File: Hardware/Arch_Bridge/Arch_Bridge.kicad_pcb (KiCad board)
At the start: 2 copper layers, 88.8 x 76 mm, 99 parts, among them J1 Conn_01x02, J3 Conn_01x04, J4 Conn_01x04, Q1 MMBT3904, Q2 MMBT3906, Q3 MJE2955, U1 AP63205WU, U10 74LVC1G04, U11 ESP32-S3-WROOM-1, U12 TXS0102DCT, U13 DRV8231ADDAR, U14 74LVC1G3208, U15 74LVC1G3208, U16 74LVC1G04, U17 TXS0102DCT, U18 TXS0102DCT, U19 TXS0108EPW, U2 TLV1117LV33DCYR, U20 TXS0108EPW, U3 LM393B, U4 74LVC1G04, U5 74LVC1G02, U6 TLP2770, U7 DRV8231ADDAR, U8 74LVC1G3208, U9 74LVC1G3208

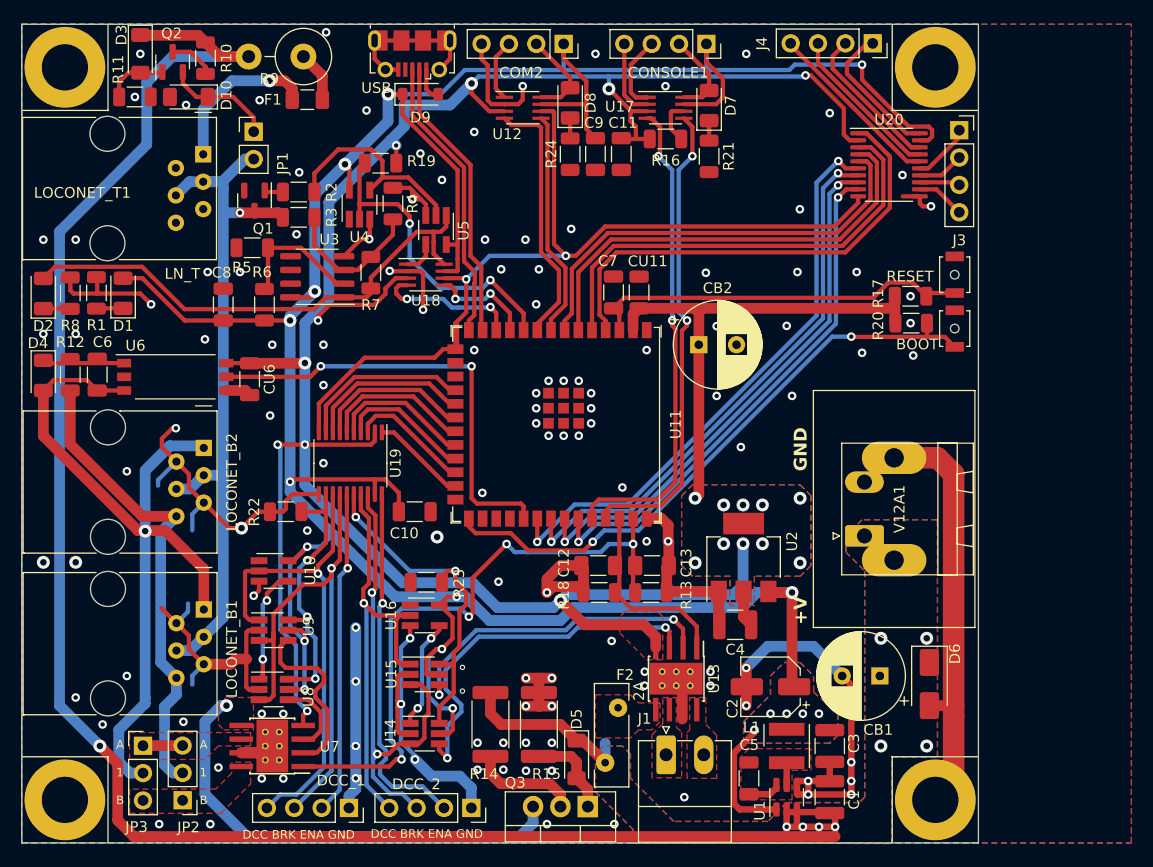
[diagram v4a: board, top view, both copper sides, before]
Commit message: Revised PCB to fix thermal problems, improve usage of board space. DCC inputs, serial ports, and GPIO all have independent IOREF connections.
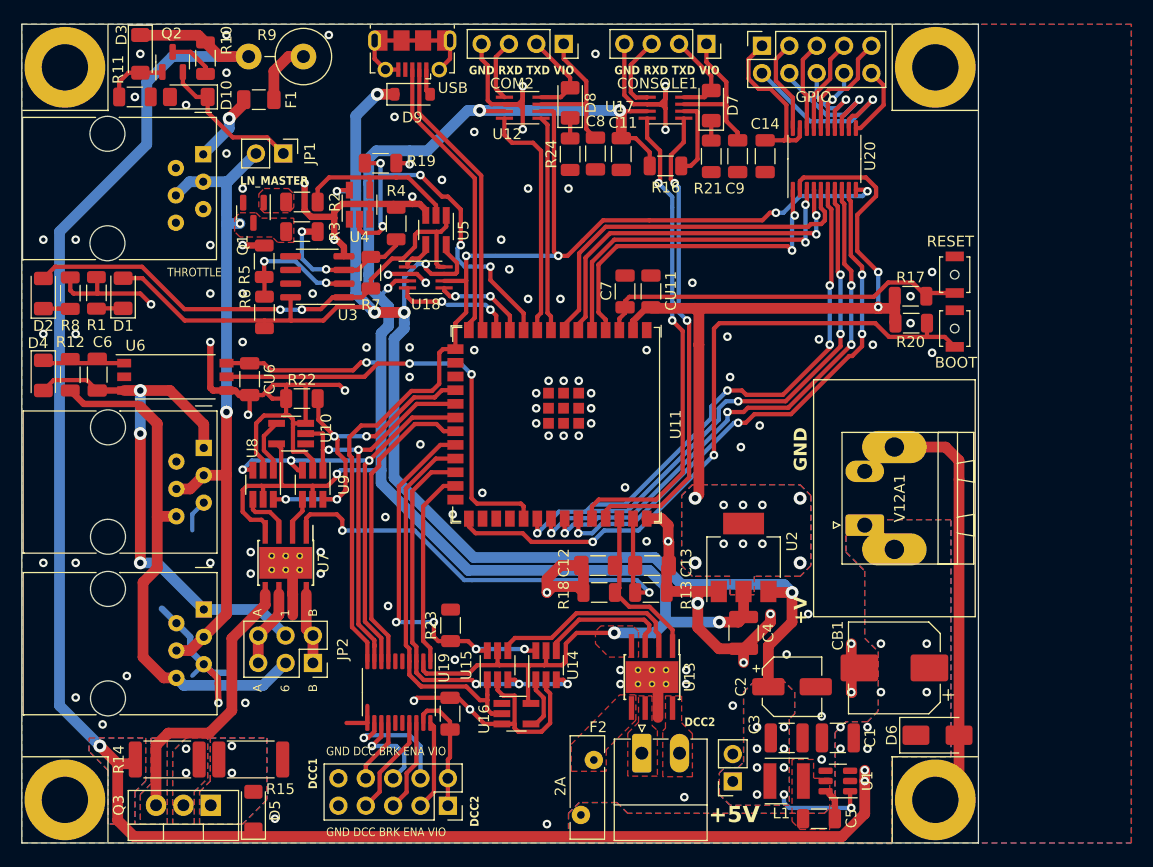
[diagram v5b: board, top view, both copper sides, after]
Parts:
- removed CB2: 100uF, Capacitor_THT:CP_Radial_D8.0mm_P3.50mm
- removed DCC_1, DCC_2: Conn_01x04_Female, Connector_PinSocket_2.54mm:PinSocket_1x04_P2.54mm_Vertical
- removed J3, J4: Conn_01x04, Connector_PinSocket_2.54mm:PinSocket_1x04_P2.54mm_Vertical
- removed JP3: Jumper_NC_Dual, Connector_PinHeader_2.54mm:PinHeader_1x03_P2.54mm_Vertical
- added C14: 0.1uF, Capacitor_SMD:C_1206_3216Metric, F.Cu at (89.0, 32.2)
- added DCC1: Conn_02x05_Odd_Even, Connector_PinSocket_2.54mm:PinSocket_2x05_P2.54mm_Vertical, F.Cu at (59.5, 92.5)
- added GPIO: Conn_02x05_Odd_Even, Connector_PinSocket_2.54mm:PinSocket_2x05_P2.54mm_Vertical, F.Cu at (88.7, 22.0)
- added J5V1: Conn_01x02, Connector_PinSocket_2.54mm:PinSocket_1x02_P2.54mm_Vertical, F.Cu at (86.0, 90.3)
- CB1: footprint Capacitor_THT:CP_Radial_D8.0mm_P3.50mm -> Capacitor_SMD:CP_Elec_8x10
- JP2: value Jumper_NC_Dual -> Conn_02x03_Odd_Even; footprint Connector_PinHeader_2.54mm:PinHeader_1x03_P2.54mm_Vertical -> Connector_PinSocket_2.54mm:PinSocket_2x03_P2.54mm_Vertical
- moved C8 37.3 mm to (73.2, 32.0), turned to -90 degrees
- moved Q3 35.0 mm to (37.5, 92.5)
- moved D5 30.4 mm to (41.5, 93.0), turned to 90 degrees
- moved R14 30.2 mm to (33.5, 88.2), turned to 180 degrees
- moved R15 26.9 mm to (41.2, 88.2), turned to 0 degrees
- moved U19 21.7 mm to (55.0, 82.0)
- moved C10 19.0 mm to (59.8, 84.0), turned to 90 degrees
- moved U8 19.0 mm to (42.4, 62.8), turned to -90 degrees
- moved JP2 17.6 mm to (47.0, 79.3), turned to -90 degrees
- moved U7 17.0 mm to (44.5, 70.0), turned to -90 degrees
- moved U9 14.0 mm to (47.0, 62.8), turned to -90 degrees
- moved C9 13.2 mm to (86.5, 32.2)
- moved U14 12.9 mm to (68.7, 79.5), turned to 90 degrees
- moved U10 12.9 mm to (45.0, 58.0), turned to 180 degrees
- moved U16 12.5 mm to (65.9, 84.0)
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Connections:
- C10 pad 1: +5V -> Net-(DCC1-Pin_1)
- C7 pad 1: /RESET -> GND
- C7 pad 2: GND -> /RESET
- C8 pad 1: +5V -> /VCOM2
- C9 pad 1: +5V -> /VCOM1
- COM2 pad 1: +5V -> /VCOM2
- CONSOLE1 pad 1: +5V -> /VCOM1
- D2 pad 2: Net-(D2-A) -> /LN_RX
- JP2 pad 2: /LN_B6 -> /OUT1_B
- JP2 pad 3: /OUT1_A -> /LN_B6
- R15 pad 1: GND -> Net-(D5-A)
- R15 pad 2: Net-(D5-A) -> GND
- R7 pad 1: Net-(D2-A) -> /LN_RX
- U10 pad 5: +5V -> +3.3V
- U11 pad 11: /LN_RX -> Net-(U11-GPIO18/U1RXD/ADC2_CH7/CLK_OUT3)
- U11 pad 12: /LN_COLL -> Net-(U11-GPIO8/TOUCH8/ADC1_CH7/SUBSPICS1)
- U11 pad 18: Net-(U11-GPIO10/TOUCH10/ADC1_CH9/FSPICS0/FSPIIO4/SUBSPICS0) -> /ENA_1o
- U11 pad 19: Net-(U11-GPIO11/TOUCH11/ADC2_CH0/FSPID/FSPIIO5/SUBSPID) -> /DCC_1
- U11 pad 20: Net-(U11-GPIO12/TOUCH12/ADC2_CH1/FSPICLK/FSPIIO6/SUBSPICLK) -> /BRK_1
- U11 pad 21: Net-(U11-GPIO13/TOUCH13/ADC2_CH2/FSPIQ/FSPIIO7/SUBSPIQ) -> /ENA_1i
- U11 pad 22: Net-(U11-GPIO14/TOUCH14/ADC2_CH3/FSPIWP/FSPIDQS/SUBSPIWP) -> /ENA_2o
- U11 pad 23: Net-(U11-GPIO21) -> /DCC_2
- U11 pad 24: Net-(U11-GPIO47/SPICLK_P/SUBSPICLK_P_DIFF) -> /BRK_2
- U11 pad 25: Net-(U11-GPIO48/SPICLK_N/SUBSPICLK_N_DIFF) -> /ENA_2i
- U12 pad 7: +5V -> /VCOM2
- U14 pad 5: +5V -> +3.3V
- U15 pad 5: +5V -> +3.3V
- U16 pad 5: +5V -> +3.3V
- U17 pad 7: +5V -> /VCOM1
- U18 pad 1: Net-(U18-B2) -> /LN_COLL
- U18 pad 4: /LN_COLL -> Net-(U11-GPIO8/TOUCH8/ADC1_CH7/SUBSPICS1)
- U18 pad 5: /LN_RX -> Net-(U11-GPIO18/U1RXD/ADC2_CH7/CLK_OUT3)
- U18 pad 8: Net-(D2-A) -> /LN_RX
- U19 pad 1: Net-(U11-GPIO48/SPICLK_N/SUBSPICLK_N_DIFF) -> /ENA_2i
- U19 pad 12: /ENA_1o -> Net-(DCC1-Pin_4)
- U19 pad 13: /DCC_1 -> Net-(DCC1-Pin_6)
- U19 pad 14: /BRK_1 -> Net-(DCC1-Pin_8)
- U19 pad 15: /ENA_1i -> unconnected-(U19-B5-Pad15)
- U19 pad 16: /ENA_2o -> unconnected-(U19-B4-Pad16)
- U19 pad 17: /DCC_2 -> Net-(DCC1-Pin_7)
- U19 pad 18: /BRK_2 -> Net-(DCC1-Pin_5)
- U19 pad 19: +5V -> Net-(DCC1-Pin_1)
- U19 pad 20: /ENA_2i -> Net-(DCC1-Pin_3)
- U19 pad 3: Net-(U11-GPIO47/SPICLK_P/SUBSPICLK_P_DIFF) -> /BRK_2
- U19 pad 4: Net-(U11-GPIO21) -> /DCC_2
- U19 pad 5: Net-(U11-GPIO14/TOUCH14/ADC2_CH3/FSPIWP/FSPIDQS/SUBSPIWP) -> unconnected-(U19-A4-Pad5)
- U19 pad 6: Net-(U11-GPIO13/TOUCH13/ADC2_CH2/FSPIQ/FSPIIO7/SUBSPIQ) -> unconnected-(U19-A5-Pad6)
- U19 pad 7: Net-(U11-GPIO12/TOUCH12/ADC2_CH1/FSPICLK/FSPIIO6/SUBSPICLK) -> /ENA_1i
- U19 pad 8: Net-(U11-GPIO11/TOUCH11/ADC2_CH0/FSPID/FSPIIO5/SUBSPID) -> /BRK_1
- U19 pad 9: Net-(U11-GPIO10/TOUCH10/ADC1_CH9/FSPICS0/FSPIIO4/SUBSPICS0) -> /DCC_1
- U20 pad 19: +5V -> Net-(DCC2-Pin_1)
- U3 pad 1: Net-(D2-A) -> /LN_RX
- U5 pad 1: Net-(D2-A) -> /LN_RX
- U5 pad 4: Net-(U18-B2) -> /LN_COLL
- U8 pad 5: +5V -> +3.3V
- U9 pad 5: +5V -> +3.3V
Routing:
- net +5V: track 306.5 -> 147.0 mm, vias 18 -> 15
- net Net-(D2-A): track 47.9 -> 0.00 mm
- net /LN_RX: track 9.62 -> 48.5 mm
- net /LN_B1: track 76.4 -> 51.5 mm, vias 1 -> 3
- net +12V: track 195.3 -> 172.1 mm, vias 9 -> 11
- net Net-(U13-IN1): track 35.0 -> 12.6 mm, vias 2 -> 0
- net /OE: track 83.8 -> 103.1 mm, vias 2 -> 4
- net Net-(Q3-E): track 43.5 -> 26.0 mm, vias 1 -> 0
- net Net-(U11-GPIO10/TOUCH10/ADC1_CH9/FSPICS0/FSPIIO4/SUBSPICS0): track 16.1 -> 0.00 mm
- net Net-(DCC2-Pin_1): track 0.00 -> 16.1 mm
- net /ENA_2i: track 33.9 -> 18.4 mm, vias 1 -> 0
- net Net-(U11-GPIO11/TOUCH11/ADC2_CH0/FSPID/FSPIIO5/SUBSPID): track 15.4 -> 0.00 mm
- net GND: track 287.7 -> 272.6 mm, vias 129 -> 110
- net Net-(U11-GPIO12/TOUCH12/ADC2_CH1/FSPICLK/FSPIIO6/SUBSPICLK): track 14.6 -> 0.00 mm
- net /VCOM2: track 0.00 -> 14.2 mm
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- added copper zone on F.Cu, net /LN_DAT
- added copper zone on B.Cu, net Net-(D5-A)
- added copper zone on F.Cu, net Net-(D5-A)
- added copper zone on F.Cu, net Net-(Q1-B)
- added copper zone on B.Cu, net Net-(Q3-C)
- added copper zone on F.Cu, net Net-(Q3-C)
- added copper zone on B.Cu, net Net-(Q3-E)
- removed copper zone on F.Cu, net /OUT1_A
- removed copper zone on F.Cu, net /OUT1_B
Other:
- board text added: "+5V"
- board text added: "A 6 B"
- board text added: "DCC1"
- board text added: "DCC2"
- board text added: "GND DCC BRK ENA VIO"
- board text added: "GND RXD TXD VIO"
- board text added: "LN_MASTER"
- board text added: "THROTTLE"
- board text removed: "DCC BRK ENA GND"
- board text removed: "LN_T"

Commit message: Board revision progress
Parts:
- added R25: 10k, Resistor_SMD:R_1206_3216Metric, F.Cu at (68.5, 39.8)
- CONSOLE1: value Conn_01x03 -> Conn_01x04
- D10: value Z-12 -> Z-13
- R9: value 33 2w -> 33 3w
- renumbered GPIO to DCC2
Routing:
- net GND: track 272.6 -> 296.1 mm, vias 110 -> 111
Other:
- board text added: "GPIO"

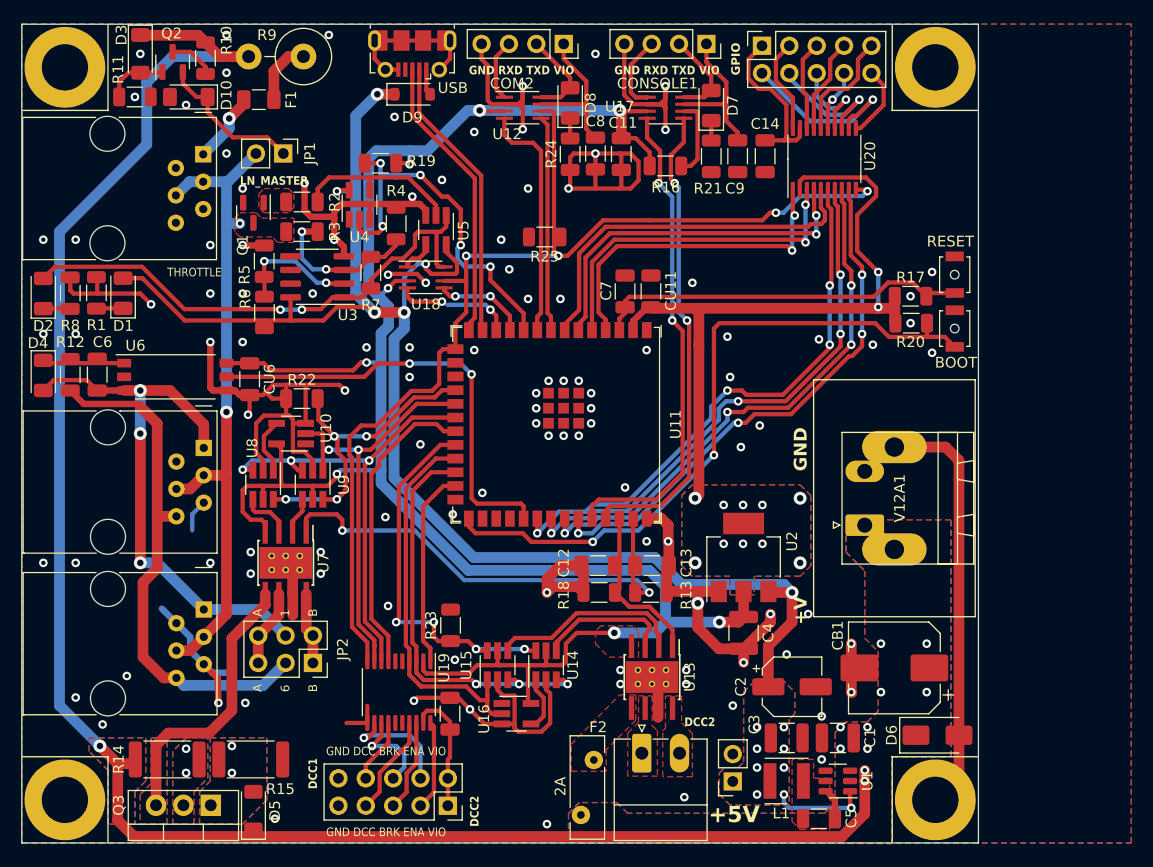
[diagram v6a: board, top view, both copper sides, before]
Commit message: Added Railsync voltage monitoring circuit, stabilizer cap. Updated BOM with new parts.
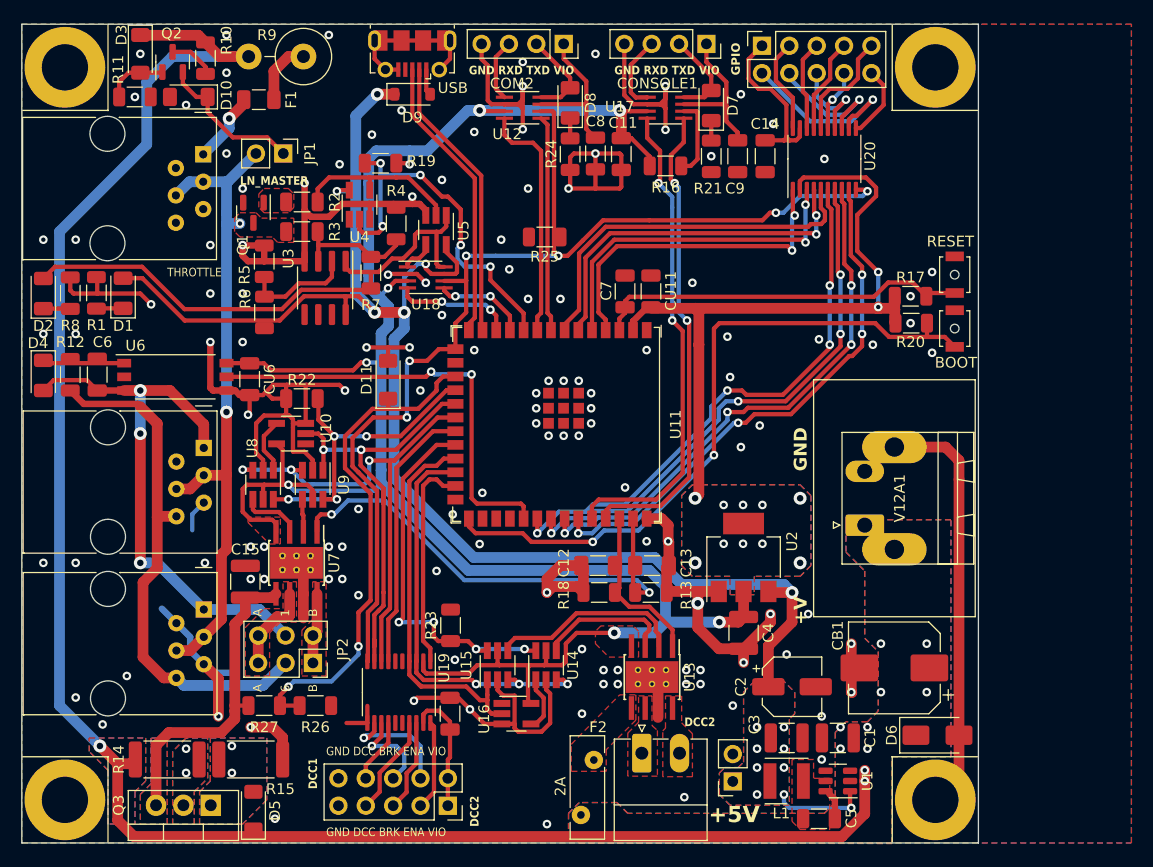
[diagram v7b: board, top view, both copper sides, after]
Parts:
- added C15: 10uF, Capacitor_SMD:C_1210_3225Metric, F.Cu at (40.8, 71.8)
- added D11: 3.3v, Diode_SMD:D_MiniMELF, F.Cu at (54.0, 53.0)
- added R26: 3k, Resistor_SMD:R_1206_3216Metric, F.Cu at (47.2, 83.2)
- added R27: 22k, Resistor_SMD:R_1206_3216Metric, F.Cu at (42.5, 83.2)
- moved U3 1.26 mm to (48.2, 44.5), turned to -90 degrees
- moved U7 1.00 mm to (45.5, 70.0)
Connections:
- net Net-(Q3-E) renamed /VM1
- net Net-(U13-VM) renamed /VM2
- U11 pad 17: unconnected-(U11-GPIO9/TOUCH9/ADC1_CH8/FSPIHD/SUBSPIHD-Pad17) -> /VMS1
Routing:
- net /VMS1: track 0.00 -> 47.3 mm, vias 0 -> 2
- net GND: track 296.1 -> 311.5 mm, vias 111 -> 128
- net /VM1: track 26.0 -> 29.8 mm
- net /LN_RX: track 48.5 -> 52.1 mm, vias 2 -> 0
- net /ENA_1i: track 28.4 -> 25.2 mm
- net Net-(U3A-+): track 14.6 -> 11.5 mm, vias 2 -> 0
- net +3.3V: track 257.8 -> 260.3 mm
- net /DCC_1: track 39.5 -> 41.6 mm
- net /ENA_2i: track 18.4 -> 20.1 mm
- net /OE: track 103.1 -> 104.7 mm, vias 4 -> 6
- net Net-(U3A--): track 11.6 -> 10.3 mm, vias 2 -> 0
- net /BRK_1: track 43.8 -> 44.9 mm
- net /OUT1_A: track 7.21 -> 8.24 mm
- net Net-(U7-IN1): track 4.82 -> 5.73 mm
- net /ENA_1o: track 30.9 -> 30.2 mm
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- added copper zone on F.Cu, net /OUT1_A
- added copper zone on F.Cu, net /OUT1_B

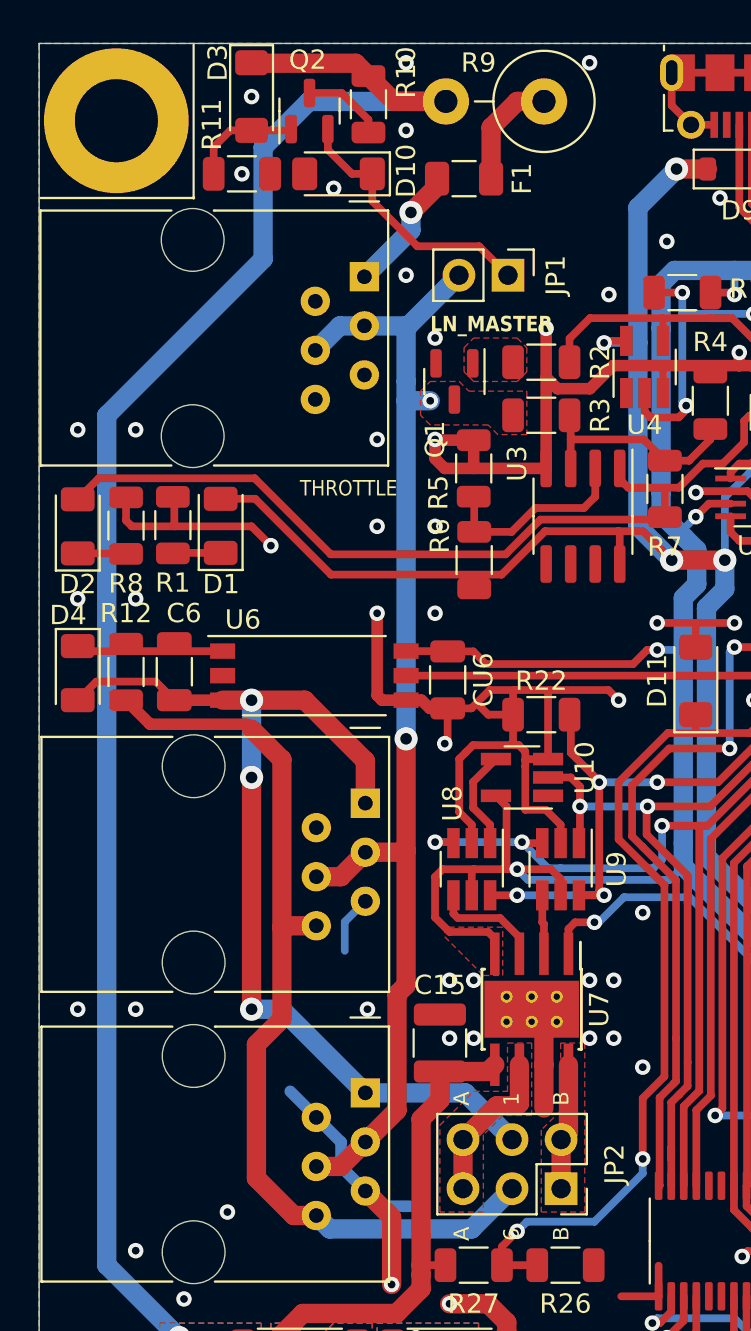
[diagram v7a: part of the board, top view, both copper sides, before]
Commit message: Fixed BOM error for JP2, should have been 2x3 pin header not socket.
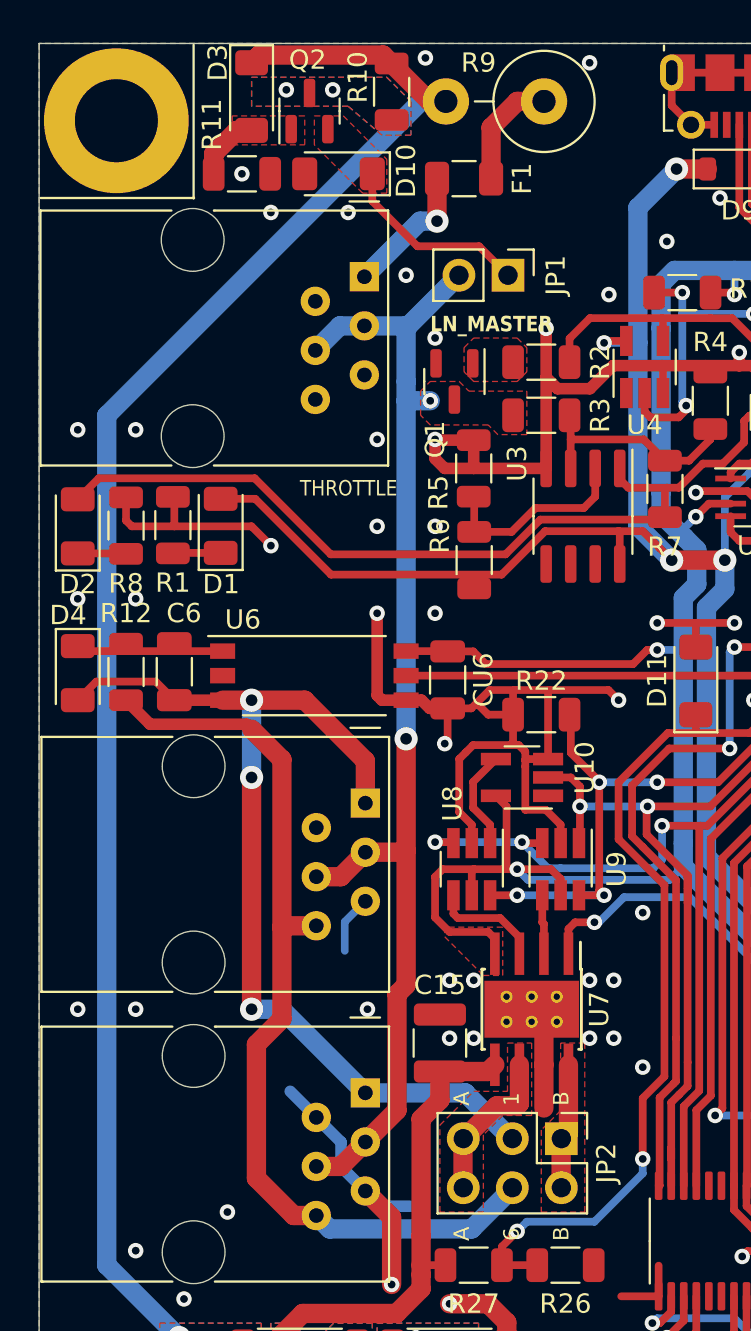
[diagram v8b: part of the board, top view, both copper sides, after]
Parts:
- JP2: footprint Connector_PinSocket_2.54mm:PinSocket_2x03_P2.54mm_Vertical -> Connector_PinHeader_2.54mm:PinHeader_2x03_P2.54mm_Vertical
- R22, R23: value 47k -> 150k
- U19, U20: value TXS0108EPW -> TXB0108PWR
- U5: value 74LVC1G02 -> 74LVC1G86
- moved JP2 2.59 mm to (47.0, 76.7)
- moved R10 1.36 mm to (38.2, 22.5)
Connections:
- JP2 pad 3: /LN_B6 -> /LN_B1
- JP2 pad 4: /LN_B1 -> /LN_B6
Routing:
- net Net-(Q2-C): track 4.29 -> 0.00 mm, vias 0 -> 2
- net Net-(D10-K): track 13.9 -> 10.0 mm
- net +12V: track 172.1 -> 169.1 mm
- net Net-(D3-A): track 5.78 -> 3.59 mm
- net /T_PWR: track 6.64 -> 7.15 mm
- net GND: vias 128 -> 127
- added copper zone on F.Cu, net Net-(D10-K)
- added copper zone on F.Cu, net Net-(D3-A)
- added copper zone on B.Cu, net Net-(Q2-C)
- added copper zone on F.Cu, net Net-(Q2-C)
